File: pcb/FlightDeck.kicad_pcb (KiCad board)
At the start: 2 copper layers, 63.3 x 35.6 mm, 4 parts, among them J1 Conn_02x08_Odd_Even_MountingP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, J2 Conn_01x19_MountingPin, J3 Conn_01x19_MountingPin, U1 ESP32-DEVKITC-32E

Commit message: New PCB and hardware details
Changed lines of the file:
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@@
 		(polygon
 			(pts
-				(xy 170.8 78.6) (xy 98.8 77.8) (xy 98.5 120.2) (xy 171.2 119.7) (xy 171.3 87.7) (xy 171.3 82.5)
+				(xy 191.4 57) (xy 58.1 55) (xy 78 143.1) (xy 194.8 134.2) (xy 197.4 89.9) (xy 211.9 75.6)
 			)
 		)

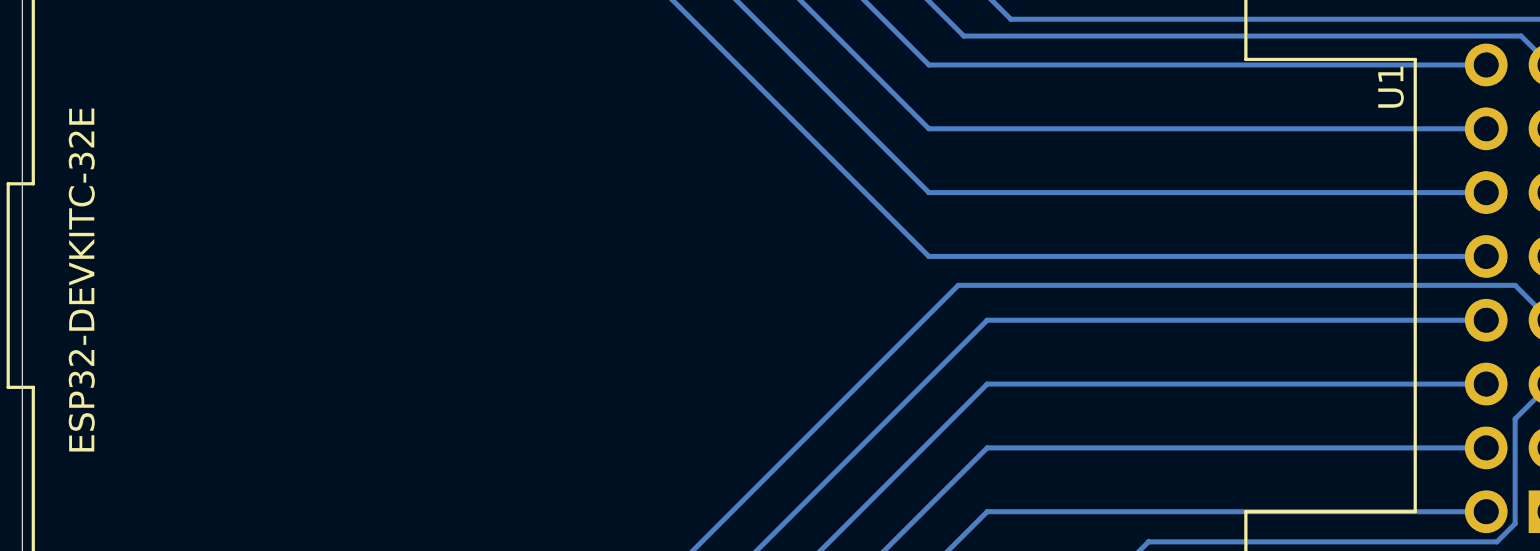
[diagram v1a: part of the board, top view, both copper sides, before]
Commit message: Update PCB with silkscreen
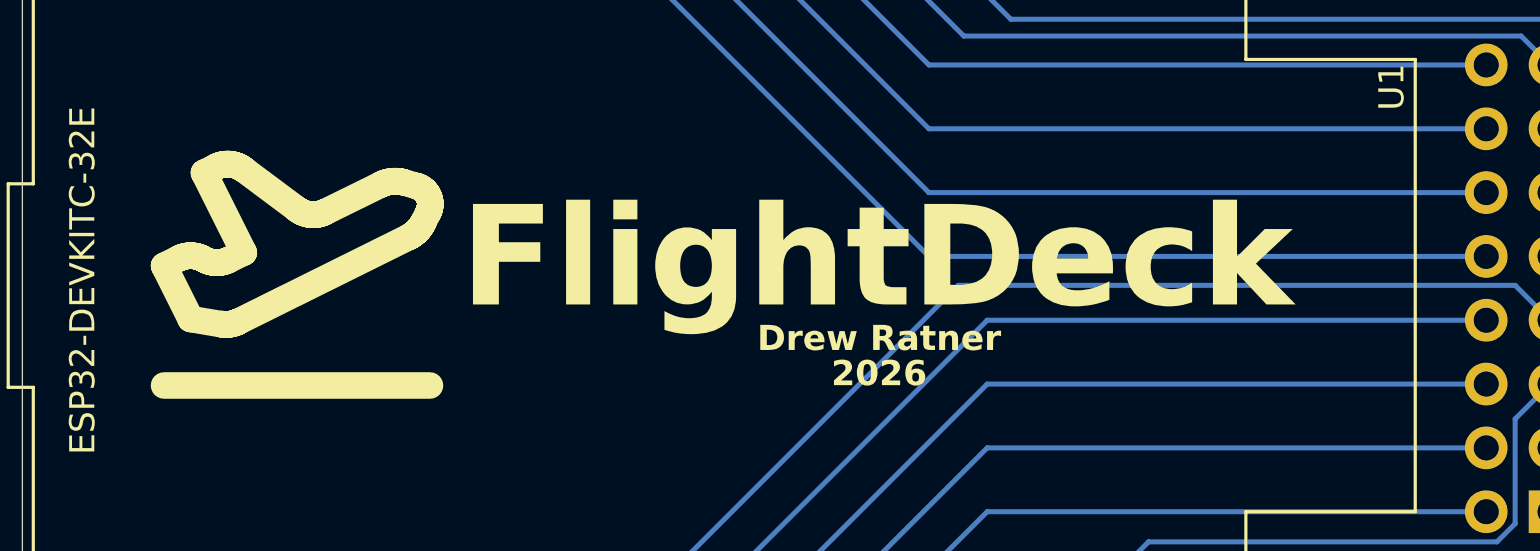
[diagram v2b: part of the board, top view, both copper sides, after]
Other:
- board text added: "11:02am"
- board text added: "1C"
- board text added: "2026"
- board text added: "5/20/2026"
- board text added: "A"
- board text added: "B71"
- board text added: "BOARDING GROUP:"
- board text added: "DATE:"
- board text added: "DEN"
- board text added: "DESTINATION:"
- board text added: "Drew Ratner"
- board text added: "F L I G H T D E C K"
- board text added: "FLIGHT:"
- board text added: "FlightDeck"
- board text added: "GATE:"
- board text added: "HC1234"
- board text added: "HKC"
- board text added: "NAME:"
- board text added: "ORIGIN:"
- board text added: "SEAT"
- board text added: "TIME:"

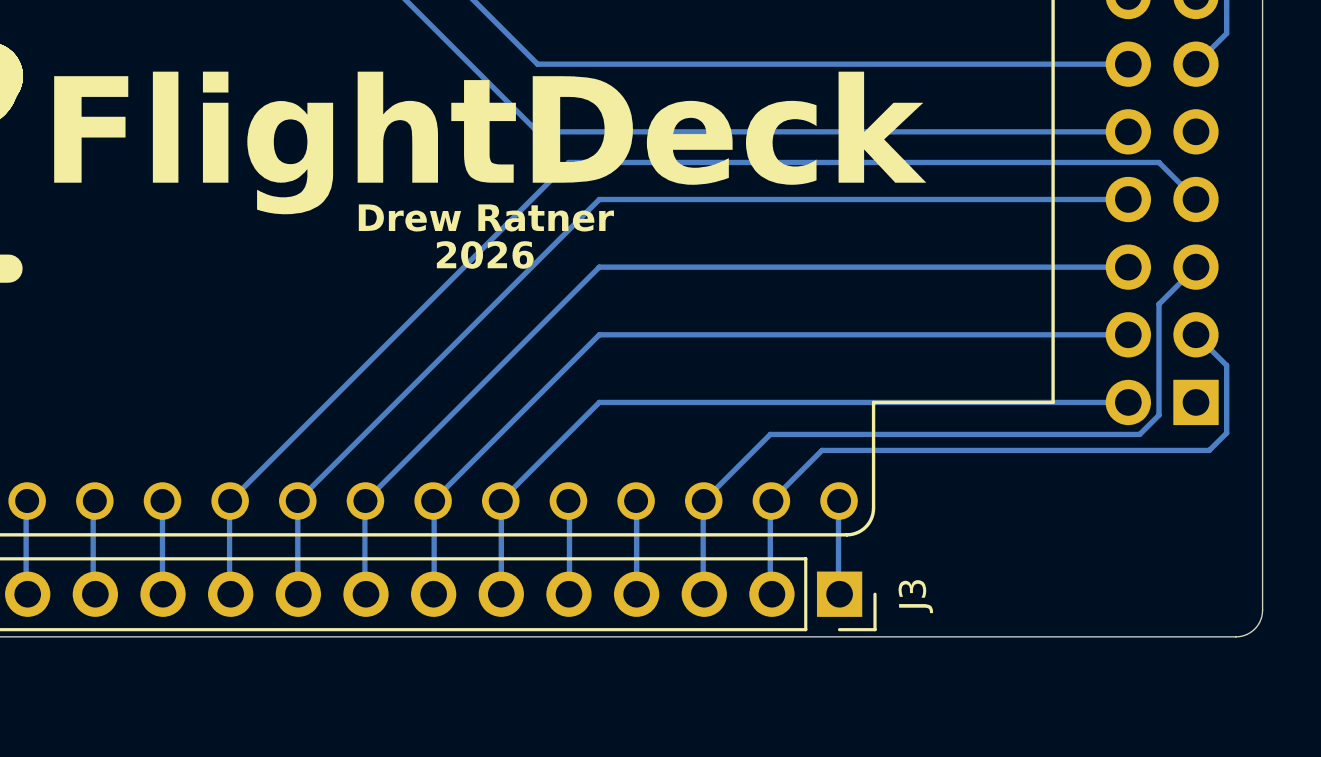
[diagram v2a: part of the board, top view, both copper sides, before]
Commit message: Updated firmware to not use circuitpython
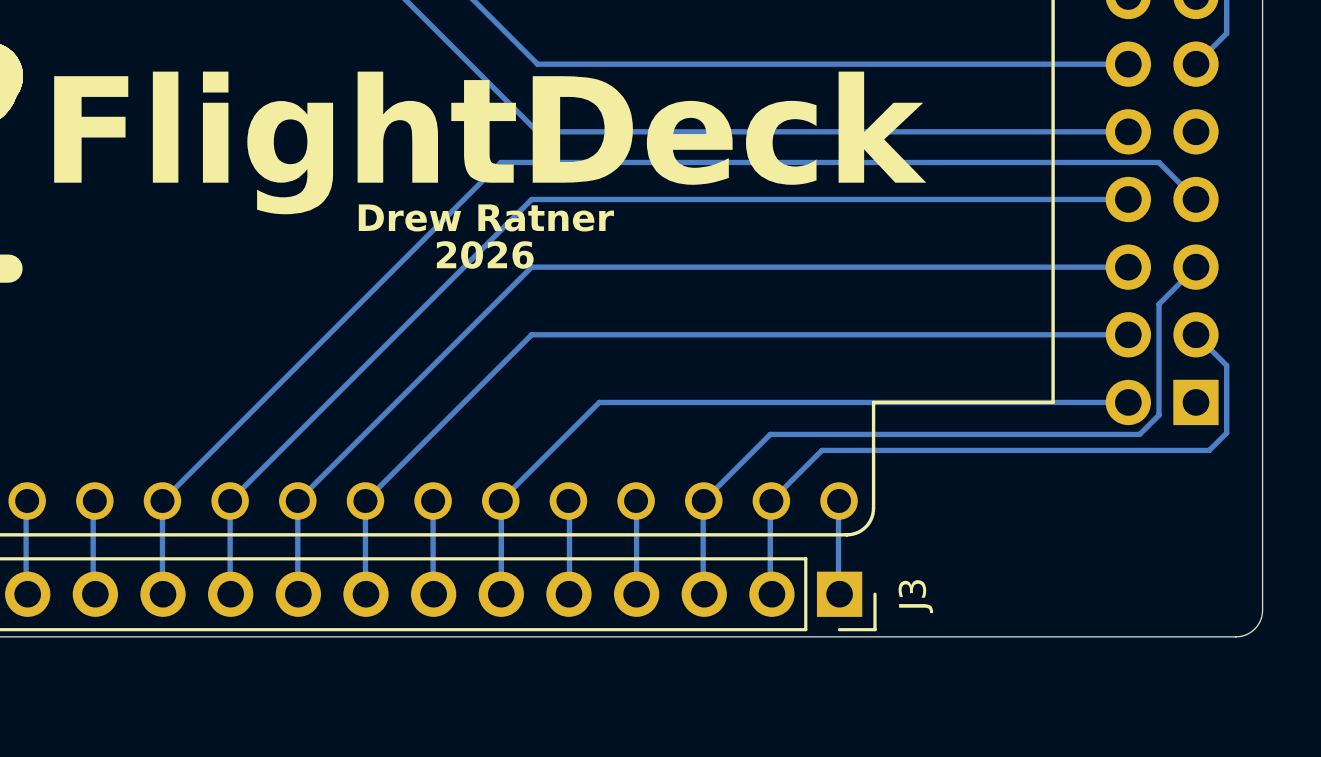
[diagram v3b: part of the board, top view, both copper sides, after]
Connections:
- J3 pad 10: B -> A
- J3 pad 11: Net-(J3-Pin_11) -> B
- J3 pad 7: CLK -> Net-(J3-Pin_7)
- J3 pad 8: C -> CLK
- J3 pad 9: A -> C
- U1 pad J3_10: B -> A
- U1 pad J3_11: Net-(J3-Pin_11) -> B
- U1 pad J3_7: CLK -> Net-(J3-Pin_7)
- U1 pad J3_8: C -> CLK
- U1 pad J3_9: A -> C
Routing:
- net Net-(J3-Pin_7): track 0.00 -> 3.51 mm
- net Net-(J3-Pin_11): track 3.48 -> 0.00 mm
- net B: track 45.6 -> 48.1 mm
- net A: track 39.3 -> 41.9 mm
- net CLK: track 32.2 -> 34.7 mm
- net C: track 35.8 -> 38.3 mm
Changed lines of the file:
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@@
 	(net 35 "Net-(J2-Pin_11)")
 	(net 36 "Net-(J3-Pin_13)")
-	(net 37 "Net-(J3-Pin_11)")
+	(net 37 "Net-(J3-Pin_7)")
 	(net 38 "Net-(J3-Pin_18)")
 	(footprint "Connector_PinSocket_2.54mm:PinSocket_1x19_P2.54mm_Vertical"
@@
 			(layers "*.Cu" "*.Mask")
 			(remove_unused_layers no)
-			(net 2 "CLK")
+			(net 37 "Net-(J3-Pin_7)")
 			(pinfunction "Pin_7")
 			(pintype "passive")
@@
 			(layers "*.Cu" "*.Mask")
 			(remove_unused_layers no)
-			(net 6 "C")
+			(net 2 "CLK")
 			(pinfunction "Pin_8")
 			(pintype "passive")
@@
 			(layers "*.Cu" "*.Mask")
 			(remove_unused_layers no)
-			(net 9 "A")
+			(net 6 "C")
 			(pinfunction "Pin_9")
 			(pintype "passive")
@@
 			(layers "*.Cu" "*.Mask")
 			(remove_unused_layers no)
-			(net 11 "B")
+			(net 9 "A")
 			(pinfunction "Pin_10")
 			(pintype "passive")
@@
 			(layers "*.Cu" "*.Mask")
 			(remove_unused_layers no)
-			(net 37 "Net-(J3-Pin_11)")
+			(net 11 "B")
 			(pinfunction "Pin_11")
 			(pintype "passive")
@@
 			(layers "*.Cu" "*.Mask")
 			(remove_unused_layers no)
-			(net 2 "CLK")
+			(net 37 "Net-(J3-Pin_7)")
 			(pinfunction "GND_J3_7")
 			(pintype "power_in")
@@
 			(layers "*.Cu" "*.Mask")
 			(remove_unused_layers no)
-			(net 6 "C")
+			(net 2 "CLK")
 			(pinfunction "IO19")
 			(pintype "bidirectional")
@@
 			(layers "*.Cu" "*.Mask")
 			(remove_unused_layers no)
-			(net 9 "A")
+			(net 6 "C")
 			(pinfunction "IO18")
 			(pintype "bidirectional")
@@
 			(layers "*.Cu" "*.Mask")
 			(remove_unused_layers no)
-			(net 11 "B")
+			(net 9 "A")
 			(pinfunction "IO5")
 			(pintype "bidirectional")
@@
 			(layers "*.Cu" "*.Mask")
 			(remove_unused_layers no)
-			(net 37 "Net-(J3-Pin_11)")
+			(net 11 "B")
 			(pinfunction "IO17")
 			(pintype "bidirectional")
@@
 		(embedded_fonts no)
 		(model "${KIPRJMOD}/lib/ESP32-DEVKITC-32E/ESP32-DEVKITC-32E.step"
-			(hide yes)
 			(offset
 				(xyz 0 0 0)
@@
 	)
 	(gr_rect
-		(start 113 100.45)
-		(end 104.6 108.65)
+		(start 104.6 100.45)
+		(end 113 108.65)
 		(stroke
 			(width 0.25)
@@
 	)
 	(segment
-		(start 161.26 104.26)
-		(end 141.4 104.26)
+		(start 132.62 113.98)
+		(end 132.64 114)
+		(width 0.2)
+		(layer "B.Cu")
+		(net 2)
+	)
+	(segment
+		(start 132.62 110.5)
+		(end 132.62 113.98)
 		(width 0.2)
 		(layer "B.Cu")
@@
 	)
 	(segment
-		(start 135.2 113.96)
-		(end 135.2 110.48)
+		(start 161.26 104.26)
+		(end 138.86 104.26)
 		(width 0.2)
 		(layer "B.Cu")
@@
 	)
 	(segment
-		(start 141.4 104.26)
-		(end 135.16 110.5)
+		(start 138.86 104.26)
+		(end 132.62 110.5)
 		(width 0.2)
 		(layer "B.Cu")
@@
 	)
 	(segment
-		(start 132.6 110.5)
-		(end 132.6 113.98)
+		(start 130.08 110.5)
+		(end 130.08 113.98)
 		(width 0.2)
 		(layer "B.Cu")
@@
 	)
 	(segment
-		(start 141.4 101.72)
-		(end 132.62 110.5)
+		(start 161.26 101.72)
+		(end 138.86 101.72)
 		(width 0.2)
 		(layer "B.Cu")
@@
 	)
 	(segment
-		(start 161.26 101.72)
-		(end 141.4 101.72)
+		(start 130.08 113.98)
+		(end 130.1 114)
+		(width 0.2)
+		(layer "B.Cu")
+		(net 6)
+	)
+	(segment
+		(start 138.86 101.72)
+		(end 130.08 110.5)
 		(width 0.2)
 		(layer "B.Cu")
@@
 	)
 	(segment
-		(start 141.4 99.18)
-		(end 130.08 110.5)
+		(start 127.54 110.5)
+		(end 127.54 113.98)
 		(width 0.2)
 		(layer "B.Cu")
@@
 	)
 	(segment
-		(start 130.08 114)
-		(end 130.08 110.52)
+		(start 161.26 99.18)
+		(end 138.86 99.18)
 		(width 0.2)
 		(layer "B.Cu")
@@
 	)
 	(segment
-		(start 161.26 99.18)
-		(end 141.4 99.18)
+		(start 138.86 99.18)
+		(end 127.54 110.5)
+		(width 0.2)
+		(layer "B.Cu")
+		(net 9)
+	)
+	(segment
+		(start 127.54 113.98)
+		(end 127.56 114)
 		(width 0.2)
 		(layer "B.Cu")
@@
 	)
 	(segment
-		(start 140.249 97.791)
-		(end 127.54 110.5)
+		(start 162.411 97.791)
+		(end 137.709 97.791)
 		(width 0.2)
 		(layer "B.Cu")
@@
 	)
 	(segment
-		(start 162.411 97.791)
-		(end 140.249 97.791)
+		(start 125 113.98)
+		(end 125.02 114)
 		(width 0.2)
 		(layer "B.Cu")
@@
 	)
 	(segment
-		(start 127.52 110.5)
-		(end 127.52 113.98)
+		(start 125 110.5)
+		(end 125 113.98)
+		(width 0.2)
+		(layer "B.Cu")
+		(net 11)
+	)
+	(segment
+		(start 137.709 97.791)
+		(end 125 110.5)
 		(width 0.2)
 		(layer "B.Cu")
@@
 	)
 	(segment
-		(start 125 114)
-		(end 125 110.52)
+		(start 135.16 110.5)
+		(end 135.16 113.98)
+		(width 0.2)
+		(layer "B.Cu")
+		(net 37)
+	)
+	(segment
+		(start 135.16 113.98)
+		(end 135.18 114)
 		(width 0.2)
 		(layer "B.Cu")
